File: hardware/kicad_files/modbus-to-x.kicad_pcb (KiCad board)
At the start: 4 copper layers, 87.6 x 46.7 mm, 65 parts, among them IC1 ESP32-WROOM-32D_M113DH2800PH3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, J1 615006138421, J4 M50-3140545R, Q1 DSS4160U-7, Q2 DSS4160U-7, SW1 SW_Wuerth_450301014042, SW4 3983, U1 LM2596S-3.3, U3 MAX3485, Y1 32.768kHz

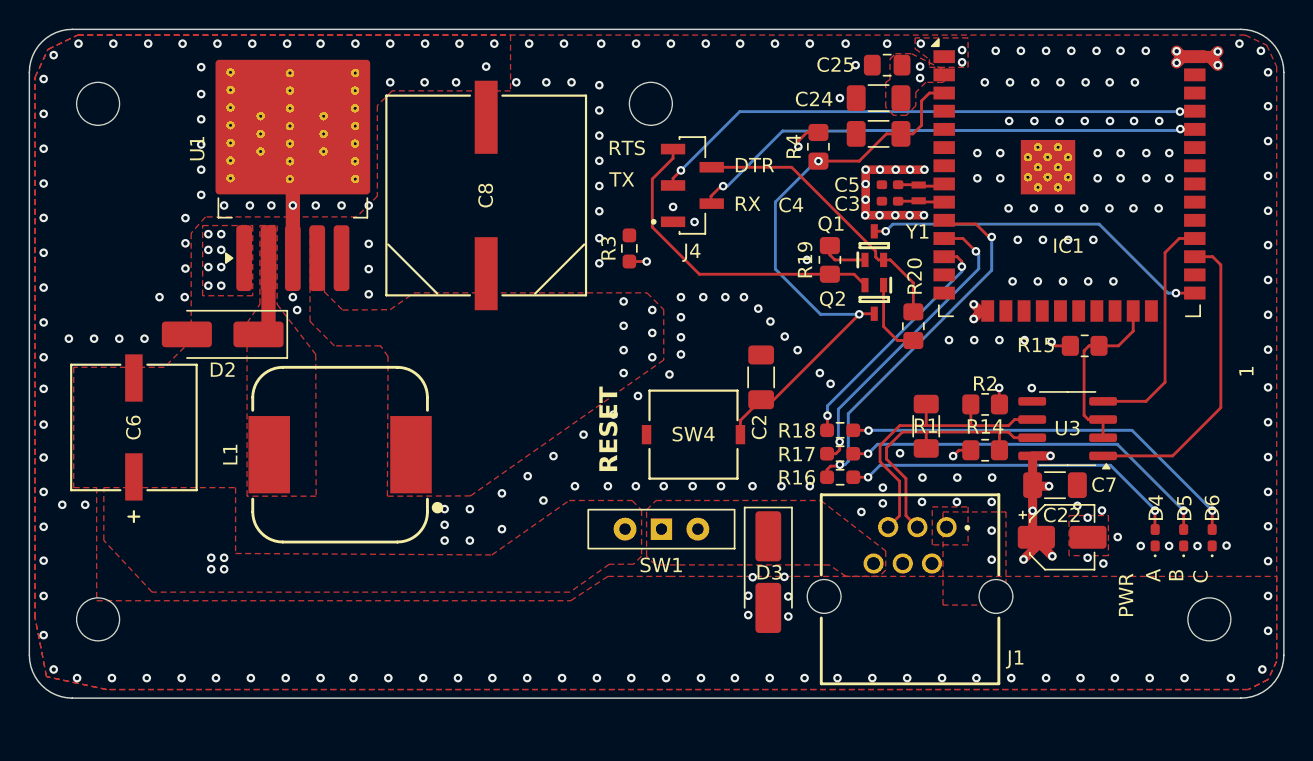
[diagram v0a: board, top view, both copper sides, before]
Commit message: lm2596 psu
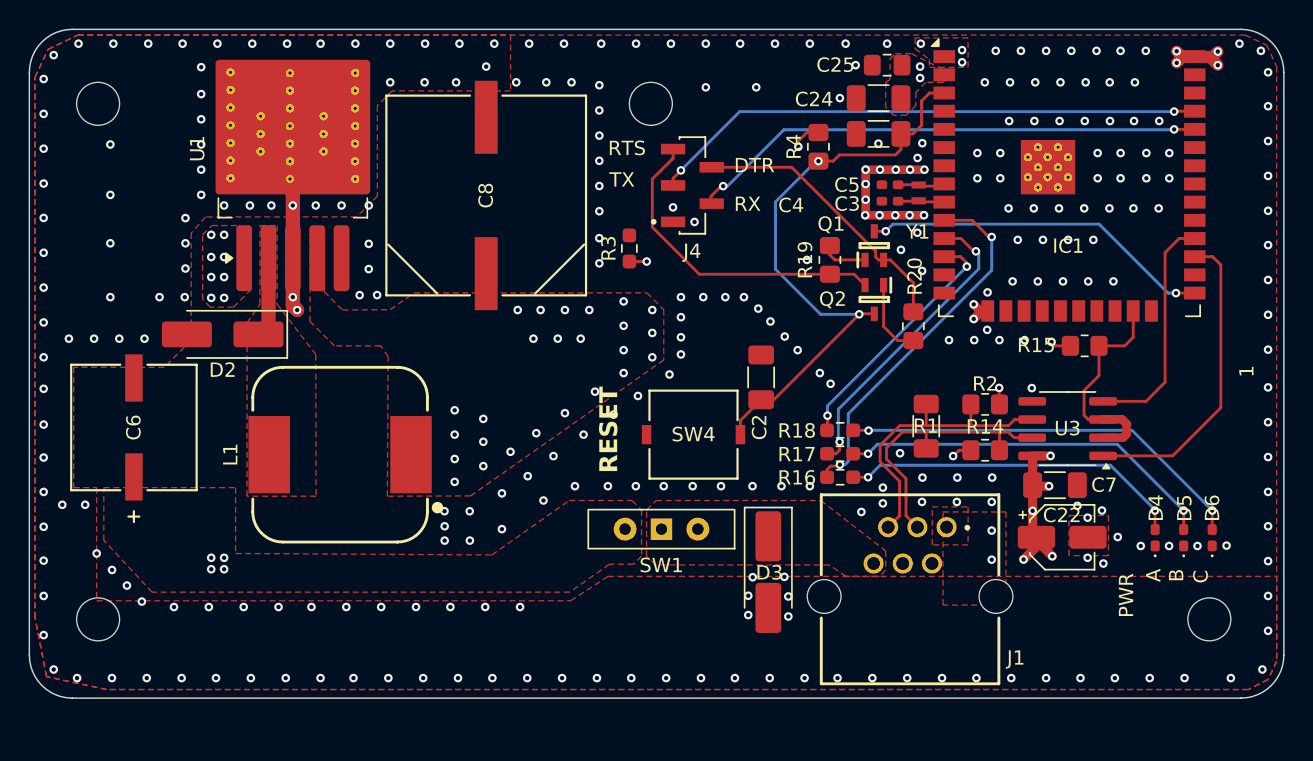
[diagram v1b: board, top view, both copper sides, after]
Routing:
- net GND: track 32.3 -> 36.1 mm, vias 287 -> 317
- net /RS485_DE_RE: track 14.0 -> 17.1 mm
- net /EN: track 41.5 -> 42.1 mm
- net VDD33: vias 17 -> 35

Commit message: improved silkscreen texts
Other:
- board text added: "A+"
- board text added: "B-"
- board text added: "GND"
- board text added: "NC"
- board text added: "VIN"
- board text added: "V_SW"

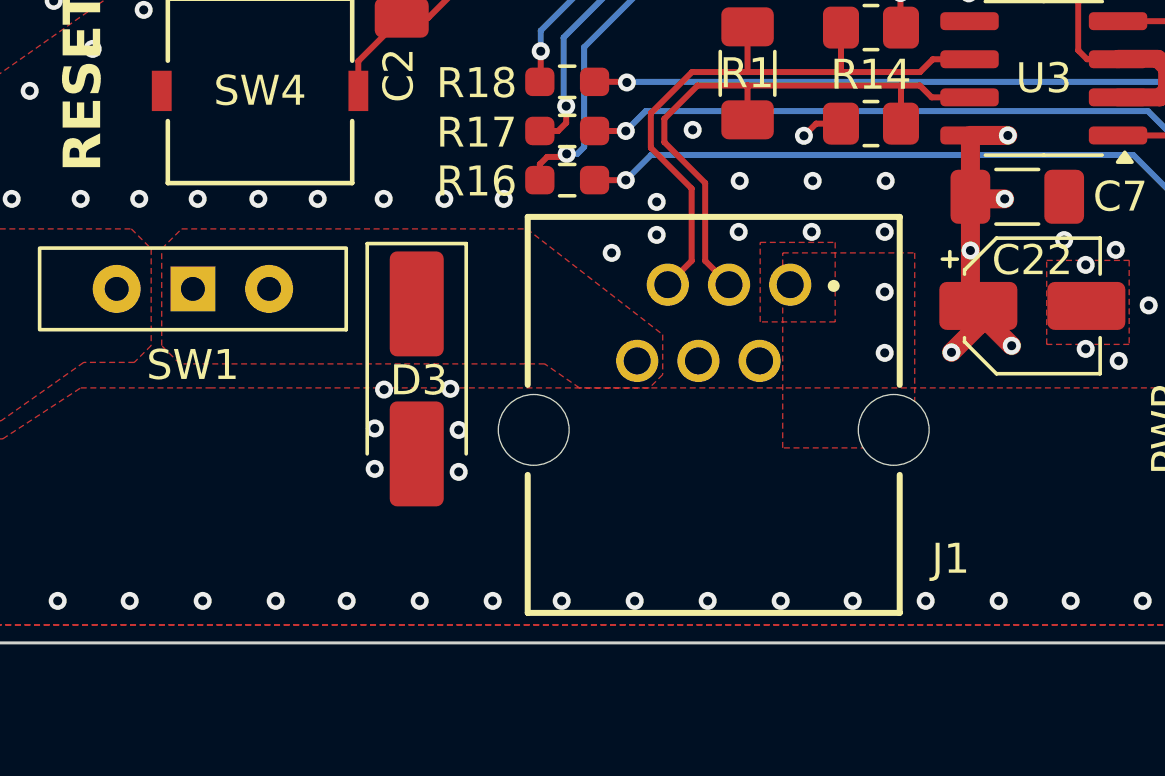
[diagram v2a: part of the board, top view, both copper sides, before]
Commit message: improved silkscreen texts cleanup
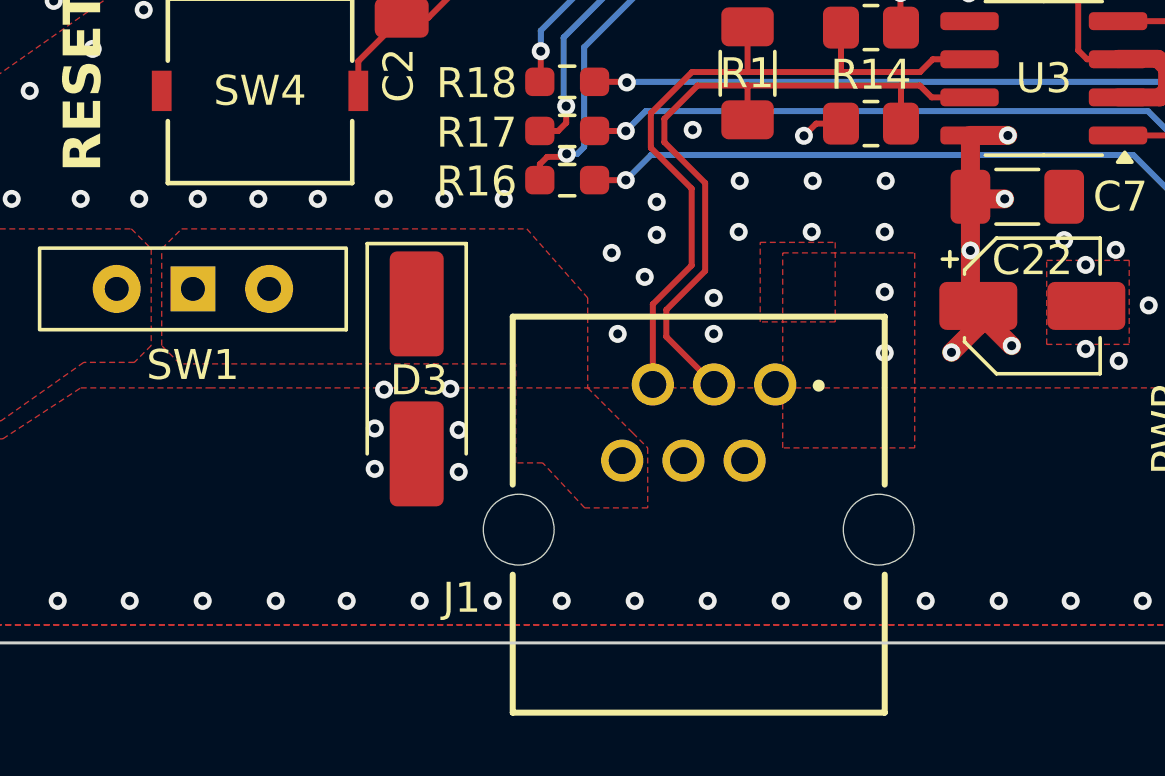
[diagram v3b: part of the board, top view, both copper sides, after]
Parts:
- moved J1 3.36 mm to (105.9, 129.9)
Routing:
- net /RS485-: track 19.6 -> 23.8 mm
- net /RS485+: track 21.0 -> 24.5 mm
- net GND: vias 317 -> 321

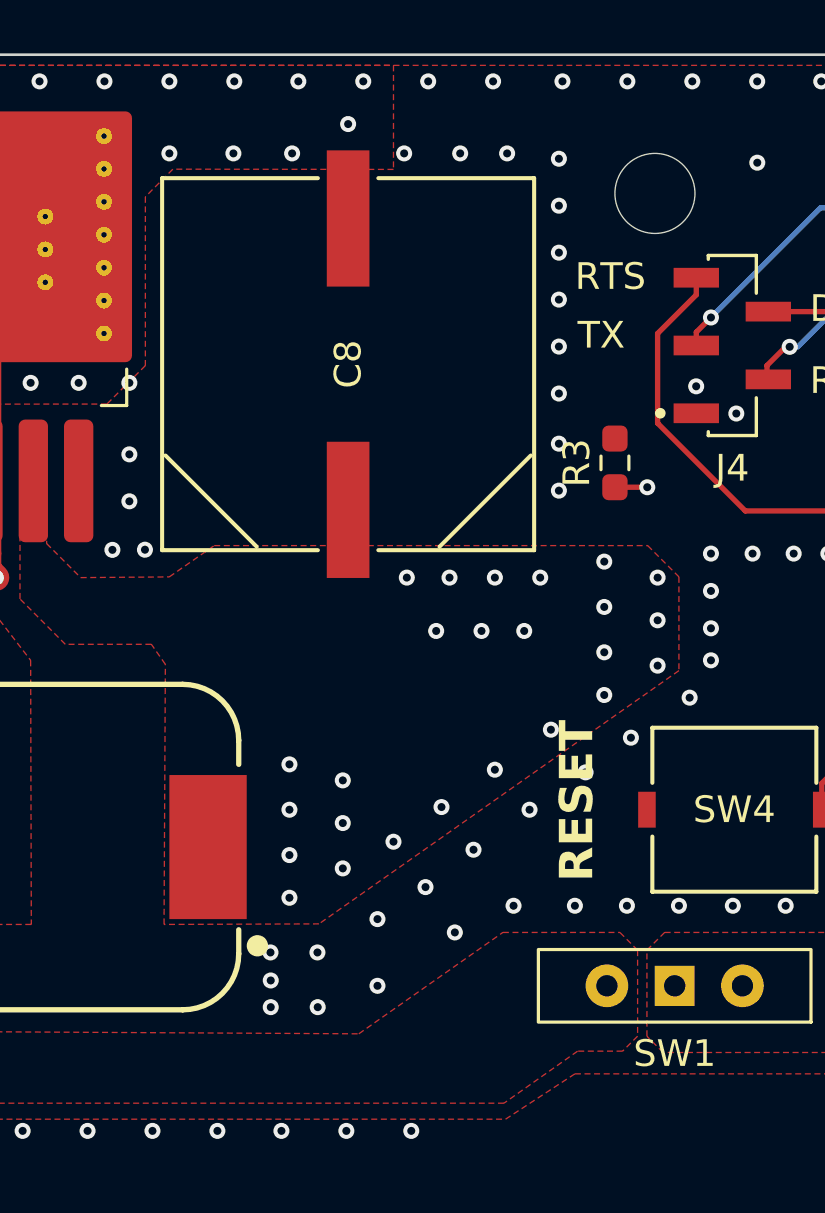
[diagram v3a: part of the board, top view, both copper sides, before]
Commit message: lm2596 output cap changed
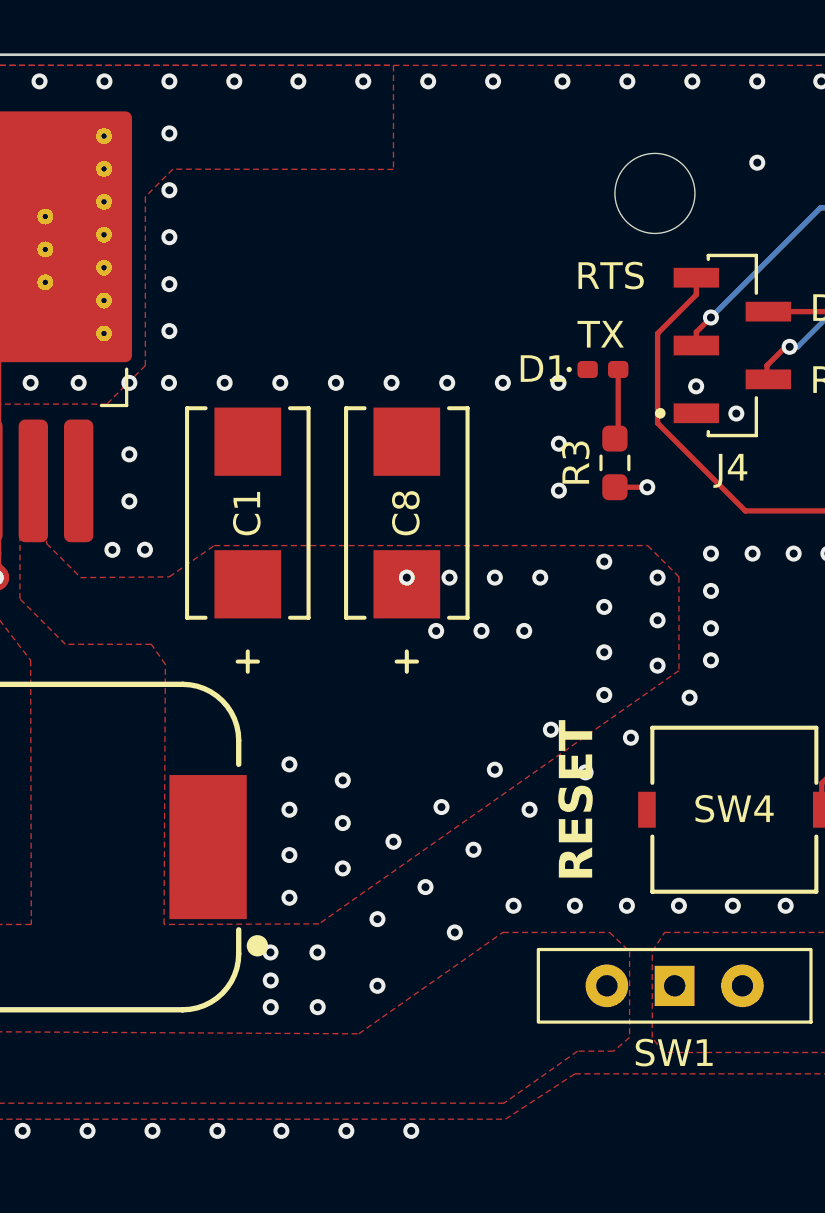
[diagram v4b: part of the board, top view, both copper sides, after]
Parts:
- added C1: 330uF, project_footprints:T495D337K006ATE100, F.Cu at (73.0, 104.7)
- added D1: PWR, LED_SMD:LED_0402_1005Metric_Pad0.77x0.64mm_HandSolder, F.Cu at (86.3, 99.3)
- C8: value 680uF -> 330uF; footprint project_footprints:EEV-FK1V681Q -> project_footprints:T495D337K006ATE100
- moved C8 6.00 mm to (79.0, 104.7)
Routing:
- net Net-(D1-A): track 0.00 -> 2.64 mm

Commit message: improved datapoint alloc. fixed indicator bug
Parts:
- D1: value PWR -> LED
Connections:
- IC1 pad 10: /LED_C -> /LED_A
- IC1 pad 12: /LED_A -> /LED_C
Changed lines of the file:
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@@
 			)
 		)
-		(property "Value" "PWR"
+		(property "Value" "LED"
 			(at -3.8 -0.05 0)
 			(layer "F.Fab")
@@
 			(size 1.5 0.9)
 			(layers "F.Cu" "F.Mask" "F.Paste")
-			(net 21 "/LED_C")
+			(net 22 "/LED_A")
 			(pinfunction "IO25")
 			(pintype "passive")
@@
 			(size 1.5 0.9)
 			(layers "F.Cu" "F.Mask" "F.Paste")
-			(net 22 "/LED_A")
+			(net 21 "/LED_C")
 			(pinfunction "IO27")
 			(pintype "passive")
@@
 		(name "$teardrop_padvia$")
 		(hatch none 0.1)
+		(priority 30002)
+		(attr
+			(teardrop
+				(type padvia)
+			)
+		)
+		(connect_pads yes
+			(clearance 0)
+		)
+		(min_thickness 0.0254)
+		(filled_areas_thickness no)
+		(fill yes
+			(thermal_gap 0.5)
+			(thermal_bridge_width 0.5)
+			(island_removal_mode 1)
+			(island_area_min 10)
+		)
+		(polygon
+			(pts
+				(xy 121.8818 108.3654) (xy 122.0818 108.3654) (xy 122.4318 107.9154) (xy 121.9818 107.1644) (xy 121.5318 107.9154)
+			)
+		)
+	)
+	(zone
+		(net 14)
+		(net_name "/RS485_DE_RE")
+		(layer "F.Cu")
+		(name "$teardrop_padvia$")
+		(hatch none 0.1)
 		(priority 30001)
 		(attr
@@
 	)
 	(zone
-		(net 6)
-		(net_name "/TX_0")
+		(net 14)
+		(net_name "/RS485_DE_RE")
 		(layer "F.Cu")
 		(name "$teardrop_padvia$")
 		(hatch none 0.1)
-		(priority 30002)
+		(priority 30000)
 		(attr
 			(teardrop
@@
 		(polygon
 			(pts
-				(xy 125.0818 93.1154) (xy 125.0818 93.3154) (xy 125.5318 93.6654) (xy 126.2828 93.2154) (xy 125.5318 92.7654)
+				(xy 119.4926 110.901) (xy 119.6926 110.901) (xy 120.17357 110.146671) (xy 119.5926 109.6) (xy 119.01163 110.146671)
 			)
 		)
@@
 		(name "$teardrop_padvia$")
 		(hatch none 0.1)
-		(priority 30000)
+		(priority 30012)
 		(attr
 			(teardrop
@@
 		(polygon
 			(pts
-				(xy 119.4926 110.901) (xy 119.6926 110.901) (xy 120.17357 110.146671) (xy 119.5926 109.6) (xy 119.01163 110.146671)
+				(xy 118.744231 114.502809) (xy 118.602809 114.644231) (xy 118.905009 114.909824) (xy 119.877907 114.746407)
+				(xy 119.0522 114.4457)
 			)
 		)
 	)
 	(zone
-		(net 14)
-		(net_name "/RS485_DE_RE")
+		(net 20)
+		(net_name "/RX_{2}")
 		(layer "F.Cu")
 		(name "$teardrop_padvia$")
 		(hatch none 0.1)
-		(priority 30012)
+		(priority 30009)
 		(attr
 			(teardrop
@@
 		(polygon
 			(pts
-				(xy 118.744231 114.502809) (xy 118.602809 114.644231) (xy 118.905009 114.909824) (xy 119.877907 114.746407)
-				(xy 119.0522 114.4457)
+				(xy 121.1522 117.3857) (xy 121.1522 117.1857) (xy 120.759603 116.997118) (xy 119.8762 117.2857)
+				(xy 120.759603 117.574282)
 			)
 		)
 	)
 	(zone
-		(net 20)
-		(net_name "/RX_{2}")
+		(net 6)
+		(net_name "/TX_0")
 		(layer "F.Cu")
 		(name "$teardrop_padvia$")
 		(hatch none 0.1)
-		(priority 30009)
+		(priority 30000)
 		(attr
 			(teardrop
@@
 		(polygon
 			(pts
-				(xy 121.1522 117.3857) (xy 121.1522 117.1857) (xy 120.759603 116.997118) (xy 119.8762 117.2857)
-				(xy 120.759603 117.574282)
+				(xy 125.0818 93.1154) (xy 125.0818 93.3154) (xy 125.5318 93.6654) (xy 126.2828 93.2154) (xy 125.5318 92.7654)
 			)
 		)
 	)
 	(zone
-		(net 1)
-		(net_name "GND")
+		(net 7)
+		(net_name "/RX_0")
 		(layer "F.Cu")
-		(hatch edge 0.5)
-		(priority 2)
+		(name "$teardrop_padvia$")
+		(hatch none 0.1)
+		(priority 30001)
+		(attr
+			(teardrop
+				(type padvia)
+			)
+		)
 		(connect_pads yes
-			(clearance 0.5)
+			(clearance 0)
 		)
-		(min_thickness 0.25)
+		(min_thickness 0.0254)
 		(filled_areas_thickness no)
 		(fill yes
 			(thermal_gap 0.5)
 			(thermal_bridge_width 0.5)
+			(island_removal_mode 1)
+			(island_area_min 10)
 		)
 		(polygon
 			(pts
-				(xy 45.300848 90.84327) (xy 46.2 88.9) (xy 48.2746 87.9) (xy 78.5 87.9) (xy 78.5 91.800108) (xy 70.230214 91.791264)
-				(xy 69.2 92.826051) (xy 69.2 99.153005) (xy 67.758018 100.595589) (xy 57.2 100.6) (xy 56.2 101.73125)
-				(xy 56.2 109.225) (xy 54.325 111.1) (xy 47.9963 111.0963) (xy 47.9963 119.5037) (xy 49.6 119.500583)
-				(xy 49.6 124.1) (xy 49.6 127.4) (xy 82.7 127.4) (xy 85.3 125.7) (xy 89.6 125.7) (xy 132 125.7) (xy 132 131.625)
-				(xy 131.4 132.9) (xy 130.025 133.6) (xy 50.3 133.6) (xy 46.1 132.7) (xy 45.300099 128.6)
+				(xy 125.0818 94.3854) (xy 125.0818 94.5854) (xy 125.5318 94.9354) (xy 126.2828 94.4854) (xy 125.5318 94.0354)
 			)
 		)
 	)
 	(zone
-		(net 14)
-		(net_name "/RS485_DE_RE")
+		(net 1)
+		(net_name "GND")
 		(layer "F.Cu")
-		(name "$teardrop_padvia$")
-		(hatch none 0.1)
-		(priority 30004)
-		(attr
-			(teardrop
-				(type padvia)
-			)
-		)
+		(hatch edge 0.5)
+		(priority 2)
 		(connect_pads yes
-			(clearance 0)
+			(clearance 0.5)
 		)
-		(min_thickness 0.0254)
+		(min_thickness 0.25)
 		(filled_areas_thickness no)
 		(fill yes
 			(thermal_gap 0.5)
 			(thermal_bridge_width 0.5)
-			(island_removal_mode 1)
-			(island_area_min 10)
 		)
 		(polygon
 			(pts
-				(xy 121.8818 108.3654) (xy 122.0818 108.3654) (xy 122.4318 107.9154) (xy 121.9818 107.1644) (xy 121.5318 107.9154)
+				(xy 45.300848 90.84327) (xy 46.2 88.9) (xy 48.2746 87.9) (xy 78.5 87.9) (xy 78.5 91.800108) (xy 70.230214 91.791264)
+				(xy 69.2 92.826051) (xy 69.2 99.153005) (xy 67.758018 100.595589) (xy 57.2 100.6) (xy 56.2 101.73125)
+				(xy 56.2 109.225) (xy 54.325 111.1) (xy 47.9963 111.0963) (xy 47.9963 119.5037) (xy 49.6 119.500583)
+				(xy 49.6 124.1) (xy 49.6 127.4) (xy 82.7 127.4) (xy 85.3 125.7) (xy 89.6 125.7) (xy 132 125.7) (xy 132 131.625)
+				(xy 131.4 132.9) (xy 130.025 133.6) (xy 50.3 133.6) (xy 46.1 132.7) (xy 45.300099 128.6)
 			)
 		)
@@
 	)
 	(zone
+		(net 22)
+		(net_name "/LED_A")
+		(layer "F.Cu")
+		(name "$teardrop_padvia$")
+		(hatch none 0.1)
+		(priority 30005)
+		(attr
+			(teardrop
+				(type padvia)
+			)
+		)
+		(connect_pads yes
+			(clearance 0)
+		)
+		(min_thickness 0.0254)
+		(filled_areas_thickness no)
+		(fill yes
+			(thermal_gap 0.5)
+			(thermal_bridge_width 0.5)
+			(island_removal_mode 1)
+			(island_area_min 10)
+		)
+		(polygon
+			(pts
+				(xy 109.895508 103.483728) (xy 110.036928 103.342308) (xy 109.5318 102.948734) (xy 108.781093 103.374693)
+				(xy 109.5318 103.8254)
+			)
+		)
+	)
+	(zone
+		(net 35)
+		(net_name "/LED_B")
+		(layer "F.Cu")
+		(name "$teardrop_padvia$")
+		(hatch none 0.1)
+		(priority 30004)
+		(attr
+			(teardrop
+				(type padvia)
+			)
+		)
+		(connect_pads yes
+			(clearance 0)
+		)
+		(min_thickness 0.0254)
+		(filled_areas_thickness no)
+		(fill yes
+			(thermal_gap 0.5)
+			(thermal_bridge_width 0.5)
+			(island_removal_mode 1)
+			(island_area_min 10)
+		)
+		(polygon
+			(pts
+				(xy 109.902947 102.195768) (xy 110.044368 102.054347) (xy 109.5318 101.667447) (xy 108.781093 102.104693)
+				(xy 109.5318 102.5554)
+			)
+		)
+	)
+	(zone
 		(net 18)
 		(net_name "/RS485+")
@@
 	)
 	(zone
+		(net 21)
+		(net_name "/LED_C")
+		(layer "F.Cu")
+		(name "$teardrop_padvia$")
+		(hatch none 0.1)
+		(priority 30003)
+		(attr
+			(teardrop
+				(type padvia)
+			)
+		)
+		(connect_pads yes
+			(clearance 0)
+		)
+		(min_thickness 0.0254)
+		(filled_areas_thickness no)
+		(fill yes
+			(thermal_gap 0.5)
+			(thermal_bridge_width 0.5)
+			(island_removal_mode 1)
+			(island_area_min 10)
+		)
+		(polygon
+			(pts
+				(xy 109.9818 100.9354) (xy 109.9818 100.7354) (xy 109.5318 100.3854) (xy 108.7808 100.8354) (xy 109.5318 101.2854)
+			)
+		)
+	)
+	(zone
 		(net 1)
 		(net_name "GND")
@@
 	)
 	(zone
-		(net 7)
-		(net_name "/RX_0")
-		(layer "F.Cu")
-		(name "$teardrop_padvia$")
-		(hatch none 0.1)
-		(priority 30003)
-		(attr
-			(teardrop
-				(type padvia)
-			)
-		)
-		(connect_pads yes
-			(clearance 0)
-		)
-		(min_thickness 0.0254)
-		(filled_areas_thickness no)
-		(fill yes
-			(thermal_gap 0.5)
-			(thermal_bridge_width 0.5)
-			(island_removal_mode 1)
-			(island_area_min 10)
-		)
-		(polygon
-			(pts
-				(xy 125.0818 94.3854) (xy 125.0818 94.5854) (xy 125.5318 94.9354) (xy 126.2828 94.4854) (xy 125.5318 94.0354)
-			)
-		)
-	)
-	(zone
 		(net 0)
 		(net_name "")
@@
 			)
 		)
-	)
-	(zone
-		(net 35)
-		(net_name "/LED_B")
-		(layer "F.Cu")
-		(name "$teardrop_padvia$")
-		(hatch none 0.1)
-		(priority 30006)
-		(attr
-			(teardrop
-				(type padvia)
-			)
-		)
-		(connect_pads yes
-			(clearance 0)
-		)
-		(min_thickness 0.0254)
-		(filled_areas_thickness no)
-		(fill yes
-			(thermal_gap 0.5)
-			(thermal_bridge_width 0.5)
-			(island_removal_mode 1)
-			(island_area_min 10)
-		)
-		(polygon
-			(pts
-				(xy 109.902947 102.195768) (xy 110.044368 102.054347) (xy 109.5318 101.667447) (xy 108.781093 102.104693)
-				(xy 109.5318 102.5554)
-			)
-		)

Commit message: customized partition table to allow fs upload without overwriting user configurations
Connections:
- IC1 pad 33: /SDA_BUS -> unconnected-(IC1-IO21-Pad33)
- IC1 pad 36: /SCL_BUS -> unconnected-(IC1-IO22-Pad36)
- R16 pad 1: /LED_C -> /LED_A
- R18 pad 1: /LED_A -> /LED_C
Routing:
- net /LED_C: track 25.9 -> 17.5 mm
- net /LED_A: track 17.5 -> 25.9 mm
